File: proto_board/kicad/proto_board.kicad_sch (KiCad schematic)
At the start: 7 parts, among them J1 pcie_98, J2 Conn_02x25_Odd_Even, J3 Conn_02x25_Odd_Even

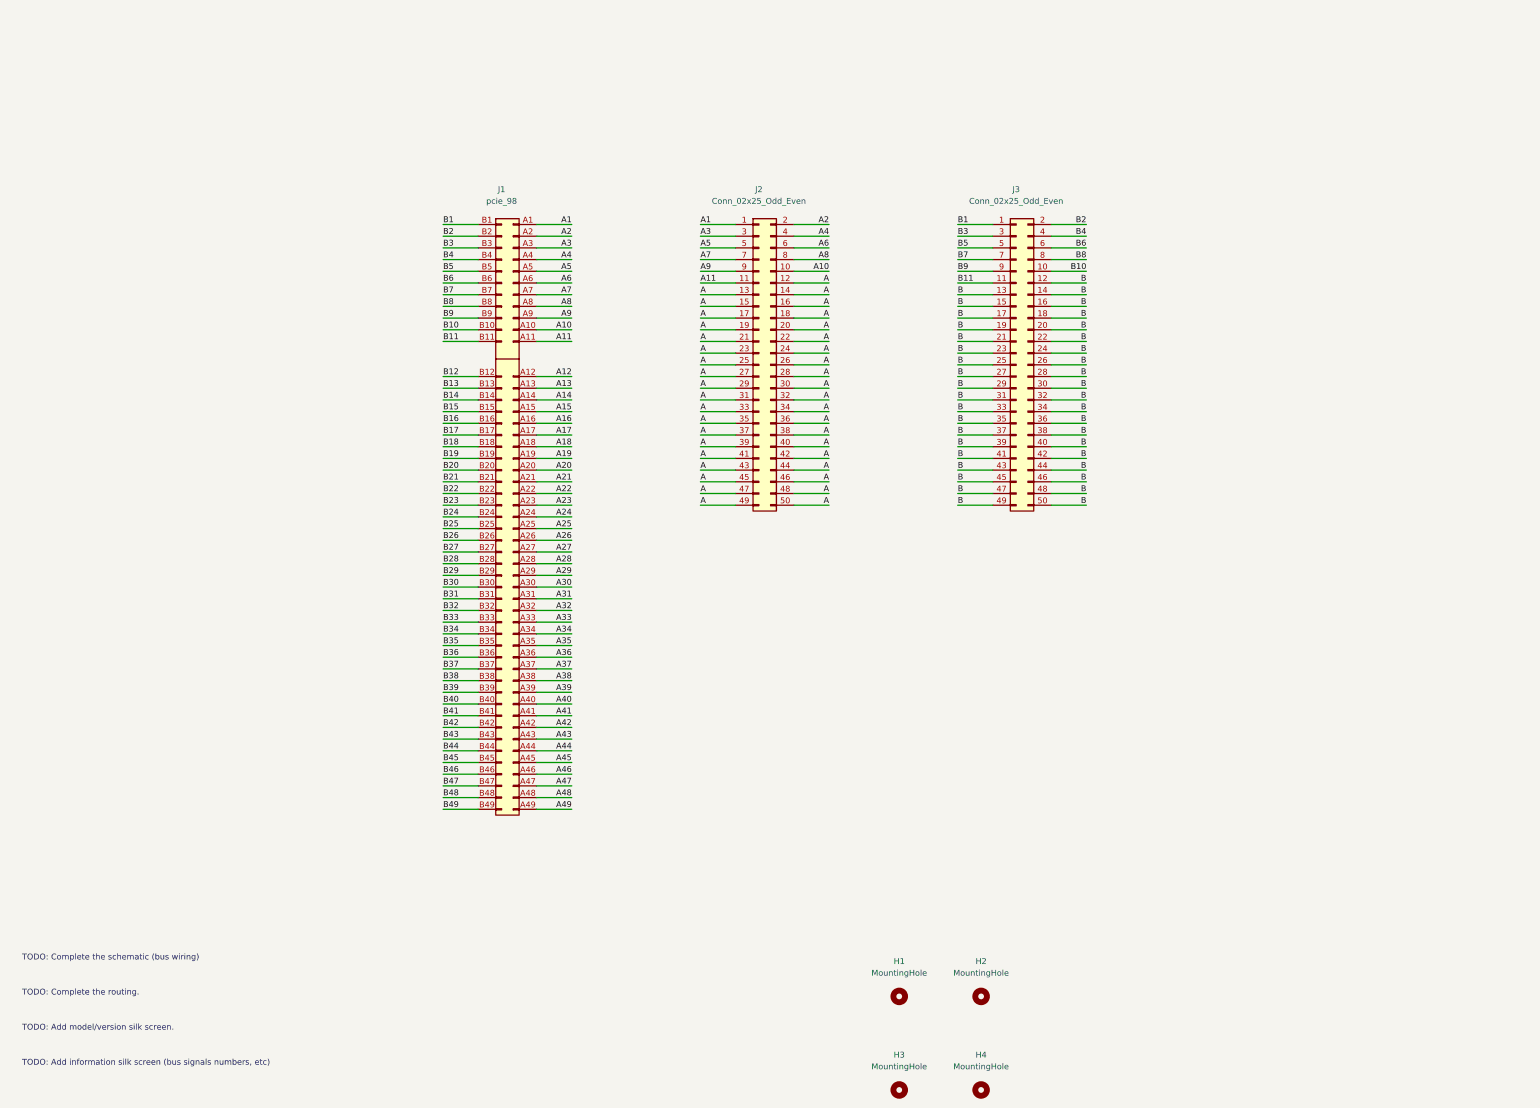
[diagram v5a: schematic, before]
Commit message: Proto board completed.
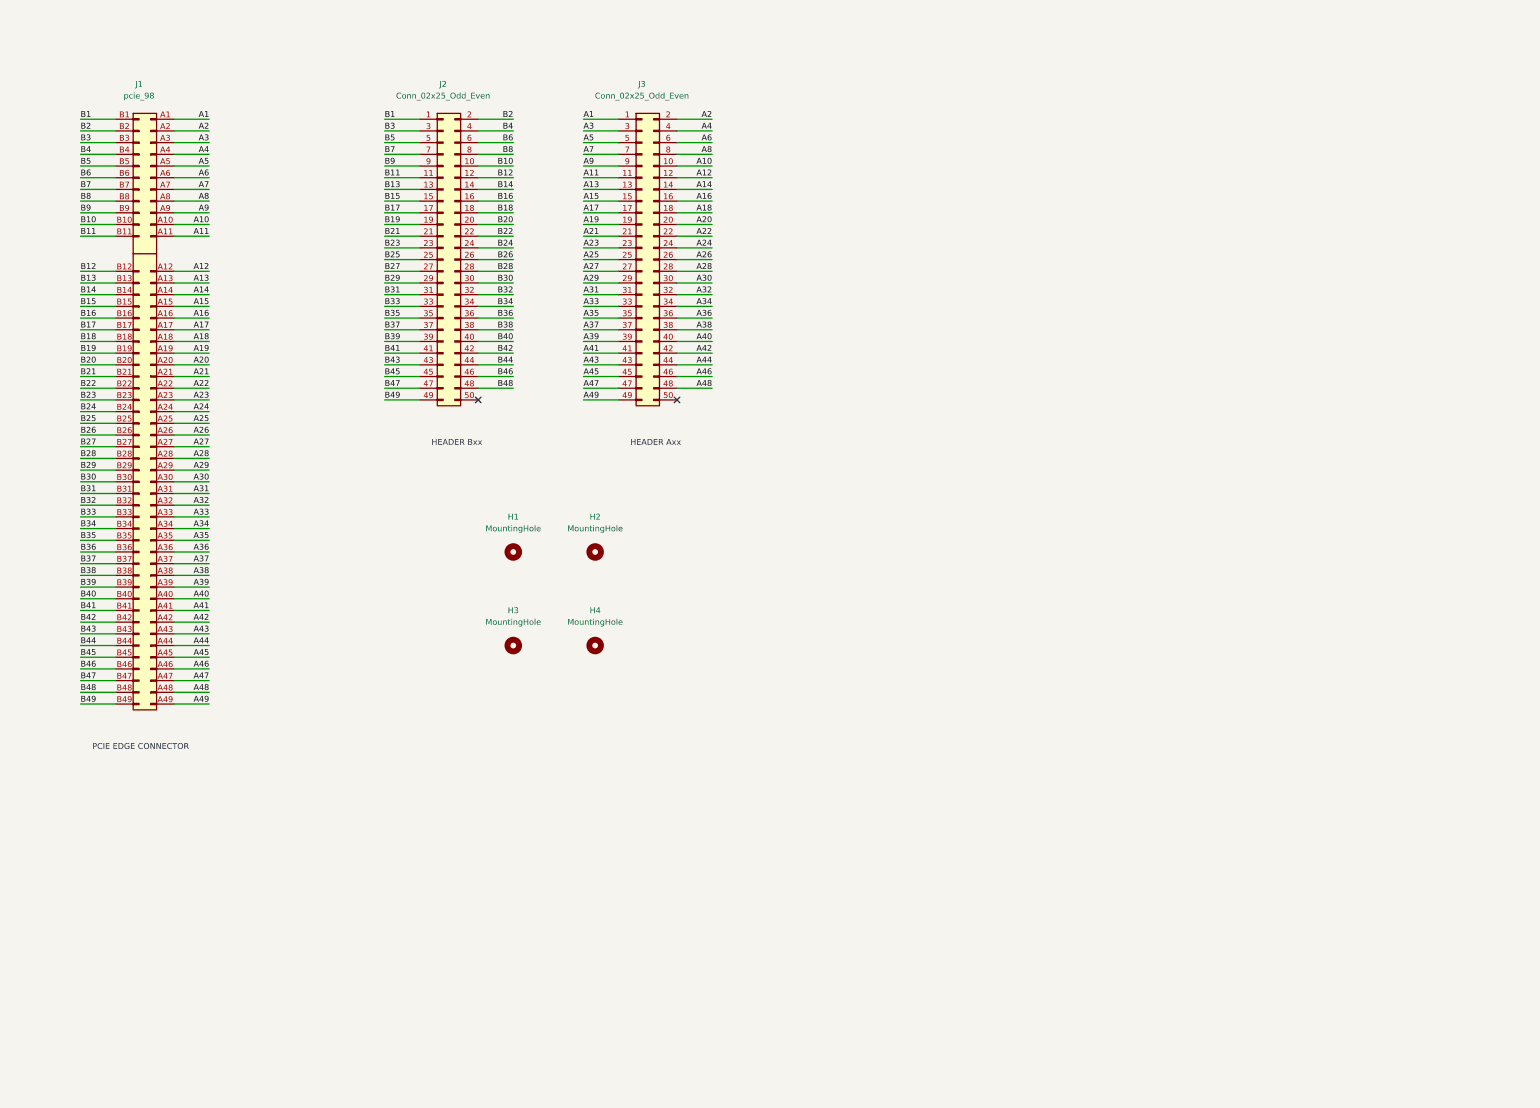
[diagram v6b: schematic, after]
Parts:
- renumbered J3 to J2, J2 to J3
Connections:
- net A12: now also J3.12 (Pin_12)
- net A13: now also J3.13 (Pin_13)
- net A14: now also J3.14 (Pin_14)
- net A15: now also J3.15 (Pin_15)
- net A16: now also J3.16 (Pin_16)
- net A17: now also J3.17 (Pin_17)
- net A18: now also J3.18 (Pin_18)
- net A19: now also J3.19 (Pin_19)
- net A20: now also J3.20 (Pin_20)
- net A21: now also J3.21 (Pin_21)
- net A22: now also J3.22 (Pin_22)
- net A23: now also J3.23 (Pin_23)
- net A24: now also J3.24 (Pin_24)
- net A25: now also J3.25 (Pin_25)
- net A26: now also J3.26 (Pin_26)
- net A27: now also J3.27 (Pin_27)
- net A28: now also J3.28 (Pin_28)
- net A29: now also J3.29 (Pin_29)
- net A30: now also J3.30 (Pin_30)
- net A31: now also J3.31 (Pin_31)
- net A32: now also J3.32 (Pin_32)
- net A33: now also J3.33 (Pin_33)
- net A34: now also J3.34 (Pin_34)
- net A35: now also J3.35 (Pin_35)
- net A36: now also J3.36 (Pin_36)
- net A37: now also J3.37 (Pin_37)
- net A38: now also J3.38 (Pin_38)
- net A39: now also J3.39 (Pin_39)
- net A40: now also J3.40 (Pin_40)
- net A41: now also J3.41 (Pin_41)
- net A42: now also J3.42 (Pin_42)
- net A43: now also J3.43 (Pin_43)
- net A44: now also J3.44 (Pin_44)
- net A45: now also J3.45 (Pin_45)
- net A46: now also J3.46 (Pin_46)
- net A47: now also J3.47 (Pin_47)
- net A48: now also J3.48 (Pin_48)
- net A49: now also J3.49 (Pin_49)
- net B12: now also J2.12 (Pin_12)
- net B13: now also J2.13 (Pin_13)
- net B14: now also J2.14 (Pin_14)
- net B15: now also J2.15 (Pin_15)
- net B16: now also J2.16 (Pin_16)
- net B17: now also J2.17 (Pin_17)
- net B18: now also J2.18 (Pin_18)
- net B19: now also J2.19 (Pin_19)
- net B20: now also J2.20 (Pin_20)
- net B21: now also J2.21 (Pin_21)
- net B22: now also J2.22 (Pin_22)
- net B23: now also J2.23 (Pin_23)
- net B24: now also J2.24 (Pin_24)
- net B25: now also J2.25 (Pin_25)
- net B26: now also J2.26 (Pin_26)
- net B27: now also J2.27 (Pin_27)
- net B28: now also J2.28 (Pin_28)
- net B29: now also J2.29 (Pin_29)
- net B30: now also J2.30 (Pin_30)
- net B31: now also J2.31 (Pin_31)
- net B32: now also J2.32 (Pin_32)
- net B33: now also J2.33 (Pin_33)
- net B34: now also J2.34 (Pin_34)
- net B35: now also J2.35 (Pin_35)
- net B36: now also J2.36 (Pin_36)
- net B37: now also J2.37 (Pin_37)
- net B38: now also J2.38 (Pin_38)
- net B39: now also J2.39 (Pin_39)
- net B40: now also J2.40 (Pin_40)
- net B41: now also J2.41 (Pin_41)
- net B42: now also J2.42 (Pin_42)
- net B43: now also J2.43 (Pin_43)
- net B44: now also J2.44 (Pin_44)
- net B45: now also J2.45 (Pin_45)
- net B46: now also J2.46 (Pin_46)
- net B47: now also J2.47 (Pin_47)
- net B48: now also J2.48 (Pin_48)
- net B49: now also J2.49 (Pin_49)
- removed net A: J3.12 (Pin_12), J3.13 (Pin_13), J3.14 (Pin_14), J3.15 (Pin_15), J3.16 (Pin_16), J3.17 (Pin_17), J3.18 (Pin_18), J3.19 (Pin_19), J3.20 (Pin_20), J3.21 (Pin_21), J3.22 (Pin_22), J3.23 (Pin_23), J3.24 (Pin_24), J3.25 (Pin_25), J3.26 (Pin_26), J3.27 (Pin_27), J3.28 (Pin_28), J3.29 (Pin_29), J3.30 (Pin_30), J3.31 (Pin_31), J3.32 (Pin_32), J3.33 (Pin_33), J3.34 (Pin_34), J3.35 (Pin_35), J3.36 (Pin_36), J3.37 (Pin_37), J3.38 (Pin_38), J3.39 (Pin_39), J3.40 (Pin_40), J3.41 (Pin_41), J3.42 (Pin_42), J3.43 (Pin_43), J3.44 (Pin_44), J3.45 (Pin_45), J3.46 (Pin_46), J3.47 (Pin_47), J3.48 (Pin_48), J3.49 (Pin_49), J3.50 (Pin_50)
- removed net B: J2.12 (Pin_12), J2.13 (Pin_13), J2.14 (Pin_14), J2.15 (Pin_15), J2.16 (Pin_16), J2.17 (Pin_17), J2.18 (Pin_18), J2.19 (Pin_19), J2.20 (Pin_20), J2.21 (Pin_21), J2.22 (Pin_22), J2.23 (Pin_23), J2.24 (Pin_24), J2.25 (Pin_25), J2.26 (Pin_26), J2.27 (Pin_27), J2.28 (Pin_28), J2.29 (Pin_29), J2.30 (Pin_30), J2.31 (Pin_31), J2.32 (Pin_32), J2.33 (Pin_33), J2.34 (Pin_34), J2.35 (Pin_35), J2.36 (Pin_36), J2.37 (Pin_37), J2.38 (Pin_38), J2.39 (Pin_39), J2.40 (Pin_40), J2.41 (Pin_41), J2.42 (Pin_42), J2.43 (Pin_43), J2.44 (Pin_44), J2.45 (Pin_45), J2.46 (Pin_46), J2.47 (Pin_47), J2.48 (Pin_48), J2.49 (Pin_49), J2.50 (Pin_50)
- no-connect marks 0 -> 2
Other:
- note added: "HEADER Axx"
- note added: "HEADER Bxx"
- note added: "PCIE EDGE CONNECTOR"
- note removed: "TODO: Add information silk screen (bus signals numbers, etc)"
- note removed: "TODO: Add model/version silk screen."
- note removed: "TODO: Complete the routing."
- note removed: "TODO: Complete the schematic (bus wiring)"
- moved on the sheet: H1, H2, H3, H4, J1, J2, J3

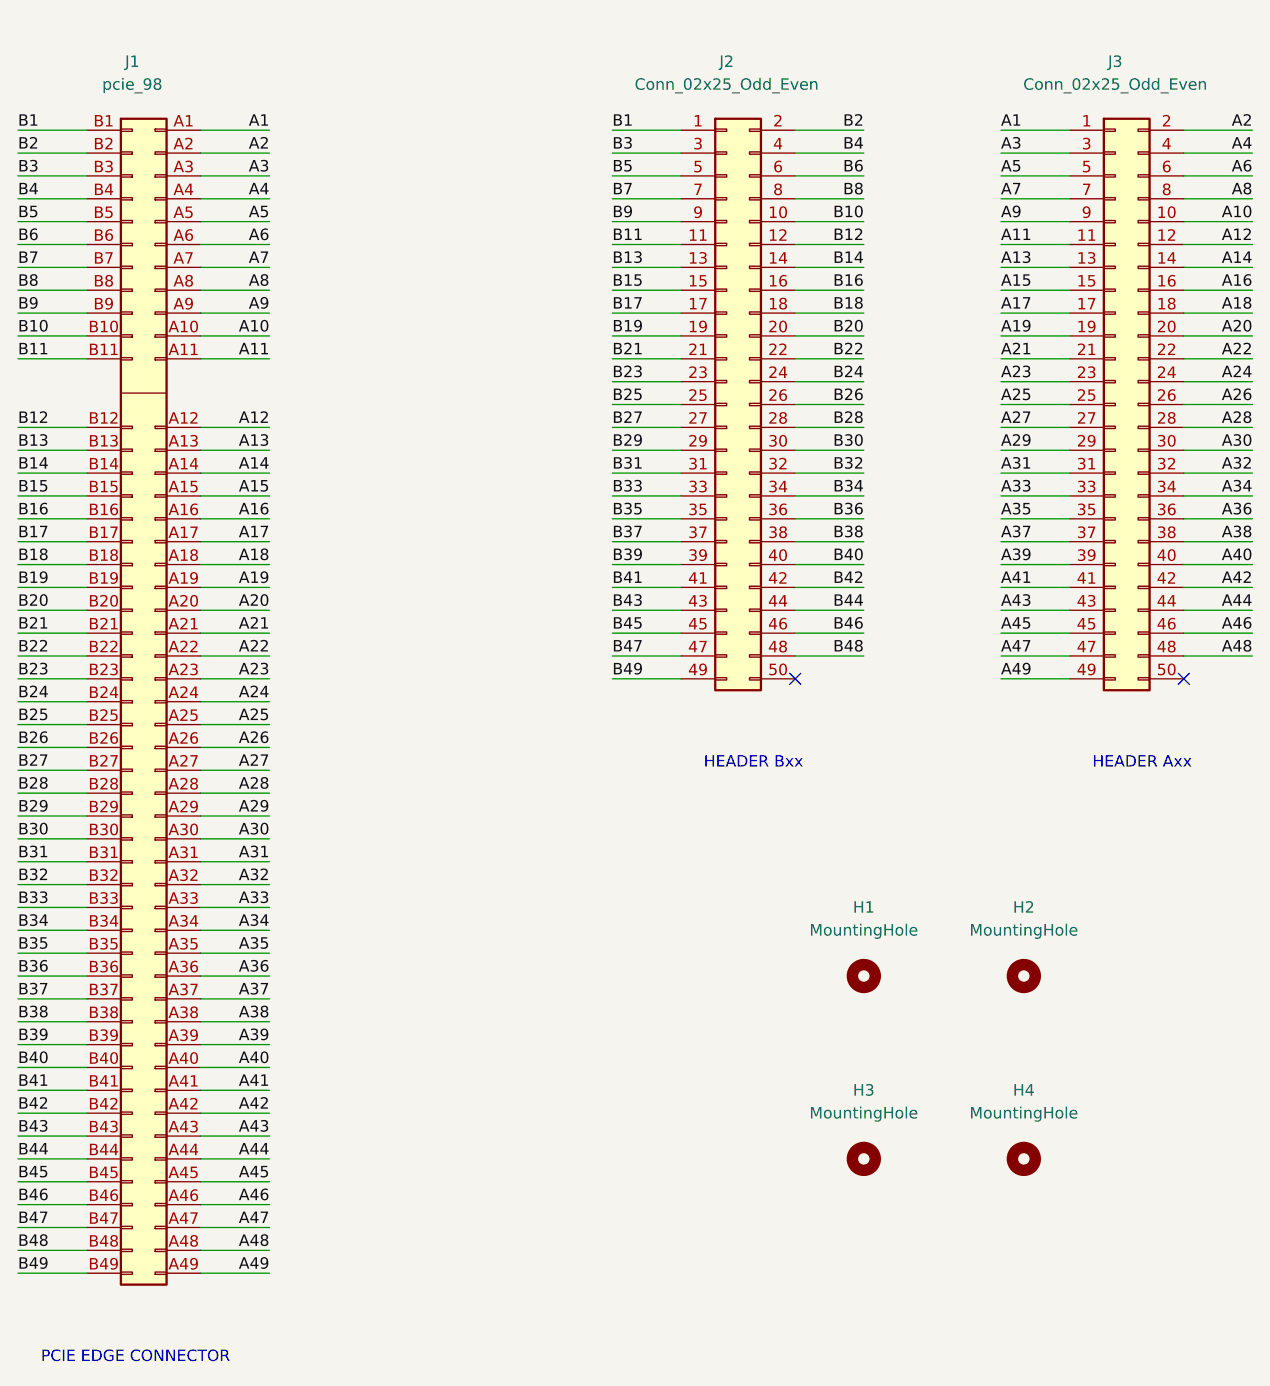
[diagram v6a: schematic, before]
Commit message: Updated the proto board with the assigned power pins.
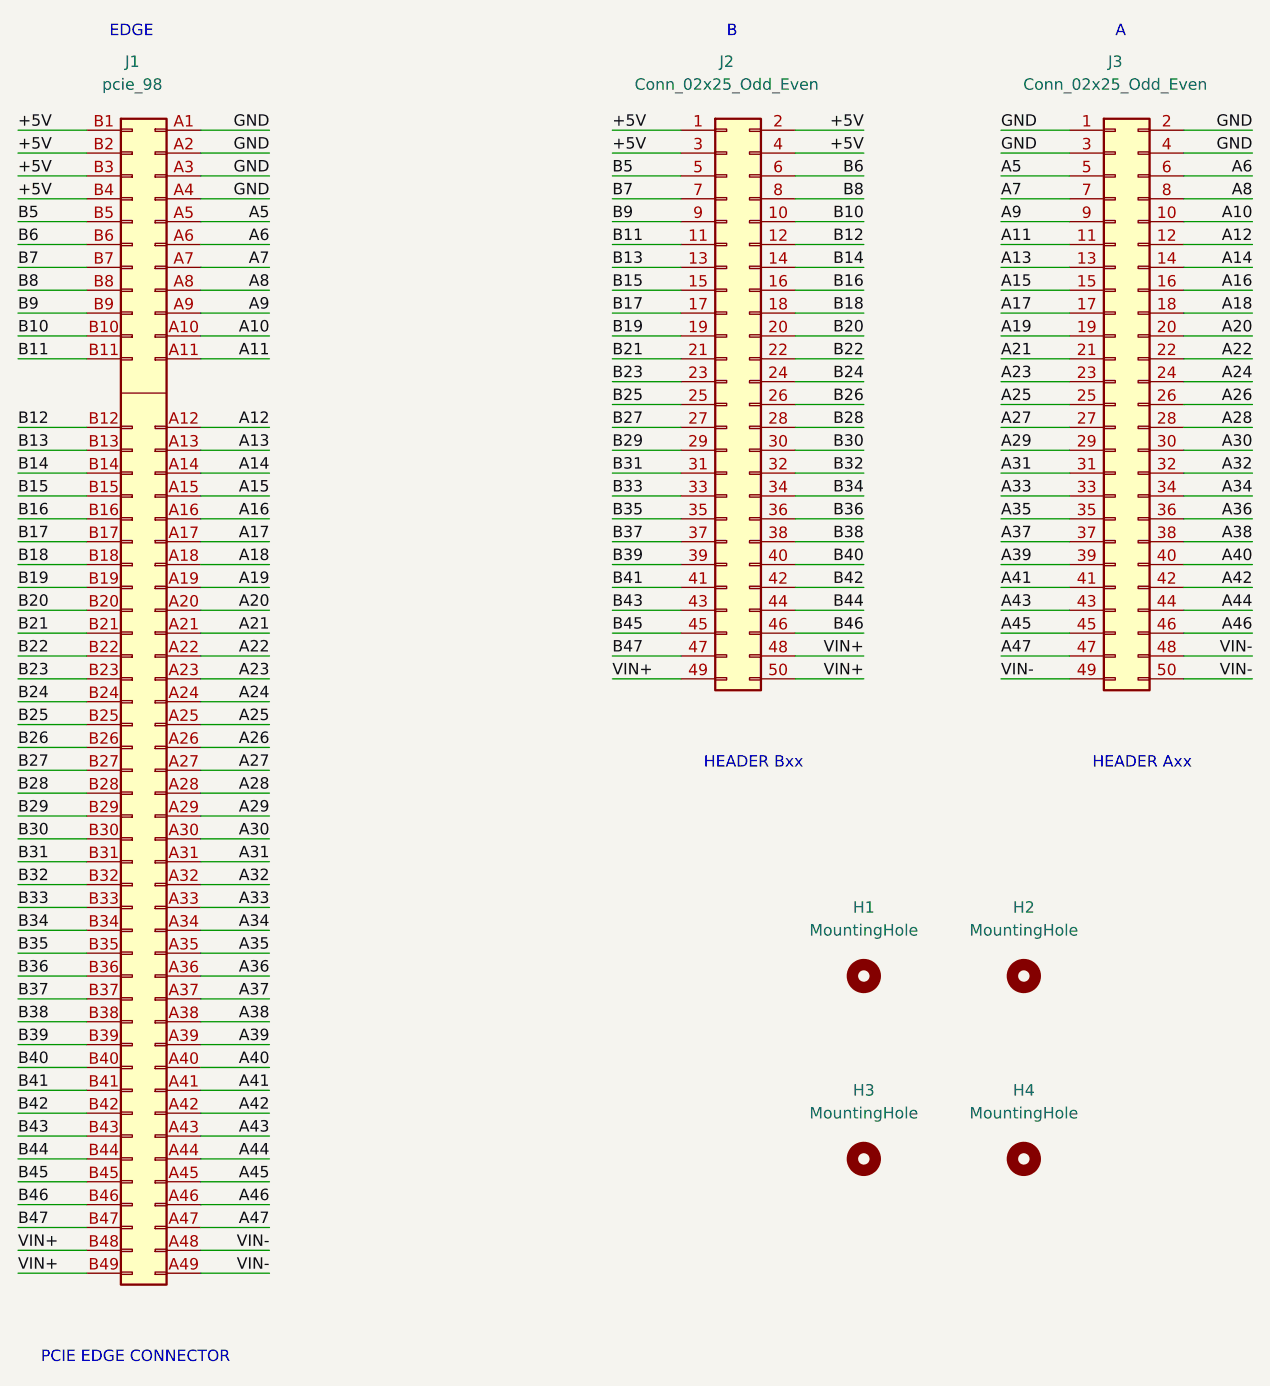
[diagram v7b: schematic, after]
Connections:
- net A2 is gone; now on net GND: J1.A2 (Pin_a2), J3.2 (Pin_2)
- net A3 is gone; now on net GND: J1.A3 (Pin_a3), J3.3 (Pin_3)
- net A4 is gone; now on net GND: J1.A4 (Pin_a4), J3.4 (Pin_4)
- net A48 is gone; now on net VIN-: J1.A48 (Pin_a48), J3.48 (Pin_48)
- net A49 is gone; now on net VIN-: J1.A49 (Pin_a49), J3.49 (Pin_49)
- net B2 is gone; now on net +5V: J1.B2 (Pin_b2), J2.2 (Pin_2)
- net B3 is gone; now on net +5V: J1.B3 (Pin_b3), J2.3 (Pin_3)
- net B4 is gone; now on net +5V: J1.B4 (Pin_b4), J2.4 (Pin_4)
- net B48 is gone; now on net VIN+: J1.B48 (Pin_b48), J2.48 (Pin_48)
- net B49 is gone; now on net VIN+: J1.B49 (Pin_b49), J2.49 (Pin_49)
- net VIN-: now reaches J3.50 (Pin_50)
- net VIN+: now reaches J2.50 (Pin_50)
- net A1 renamed GND
- net B1 renamed +5V
- no-connect marks 2 -> 0
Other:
- note added: "A"
- note added: "B"
- note added: "EDGE"
